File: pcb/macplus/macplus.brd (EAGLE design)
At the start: 58 x 35 mm, 9 parts, among them J1 ATX24RH

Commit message: mac plus adaptor pretty much done
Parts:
- added JP3: (no value), pinhead:1X02
- moved JP1 2.32 mm to (10.7, 25.3), turned to 270 degrees
- moved JP4 2.30 mm to (2.55, 25.4)
- moved U$2 0.55 mm to (46.6, 14.5)
- moved U$8 0.26 mm to (25.4, 14.5)
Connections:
- net GND: now also JP3.2
- net N$10: now also JP3.1
- net N$6: no longer J1.4
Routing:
- net -12V: track 83.6 -> 43.7 mm
- net N$10: track 9.00 -> 17.0 mm
- net +12V: track 71.2 -> 65.2 mm
- net +5V: track 53.1 -> 47.4 mm
- net N$6: track 44.5 -> 39.6 mm
- net N$8: track 14.6 -> 15.7 mm
- net N$7: track 9.40 -> 8.77 mm
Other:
- outline, holes or cut-outs redrawn
- board text added: "+12"
- board text added: "+5V"
- board text added: "-12"
- board text added: "BAT"
- board text added: "HS"
- board text added: "LATCH TOWARDS EDGE"
- board text added: "Macintosh 128K/512K/Plus ATX Adaptor PT0 dekuNukem Nov 2022"
- board text added: "SPK"
- board text added: "VID"
- board text added: "VS"
- board text removed: "3V3"
- board text removed: "Bob Dishwasher Cassette Rewinder"
- board text removed: "CART OK"
- board text removed: "CLK"
- board text removed: "DIO"
- board text removed: "DONE"
- board text removed: "G"
- board text removed: "Mac 128/512/Plus ATX Adaptor dekuNukem Nov 2022"
- board text removed: "NOTCH TOWARDS EDGE"
- board text removed: "POWER"
- board text removed: "RENEW"
- board text removed: "RESET"
- board text removed: "RX"
- board text removed: "SCL"
- board text removed: "SDA"
- board text removed: "TX"
- board text removed: "VCC"
- board text removed: "dekuNukem 2021"
- board text removed: "git.io/bob_rewind"

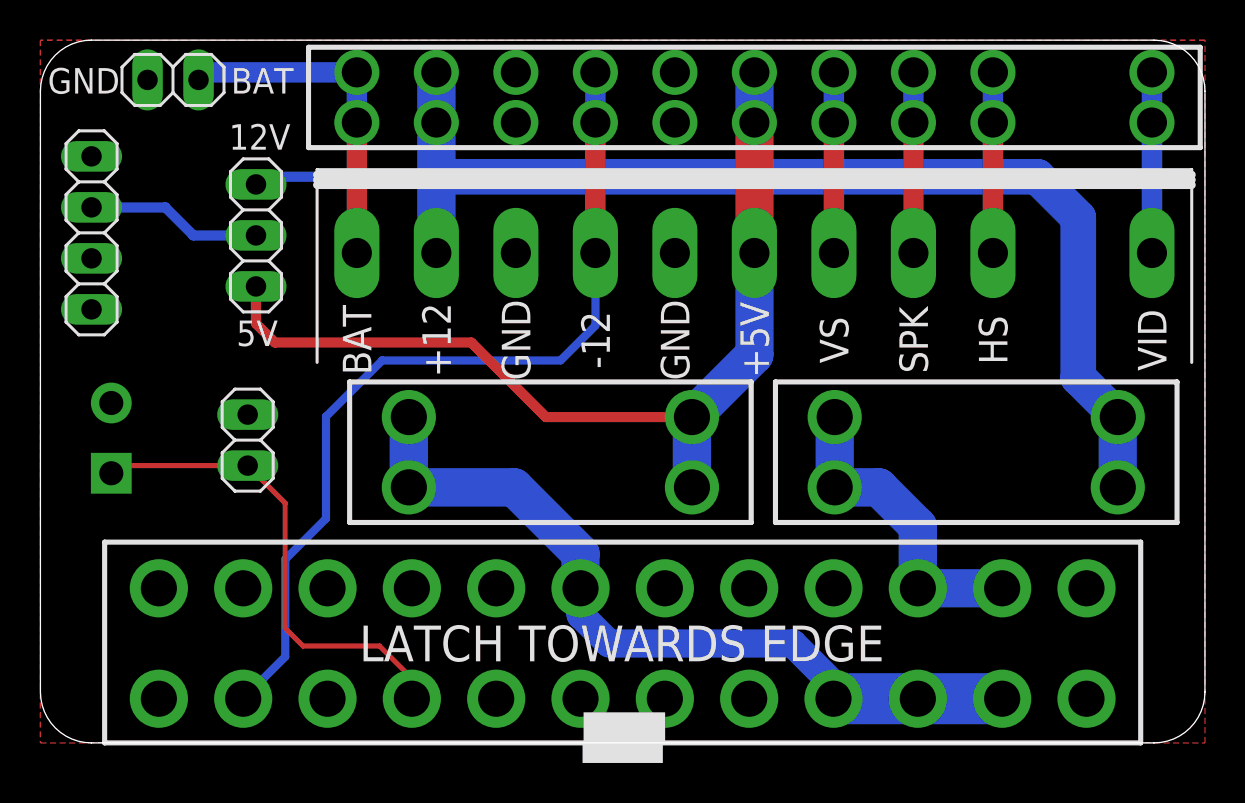
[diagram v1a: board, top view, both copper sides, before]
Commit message: updated mac plus atx adaptor
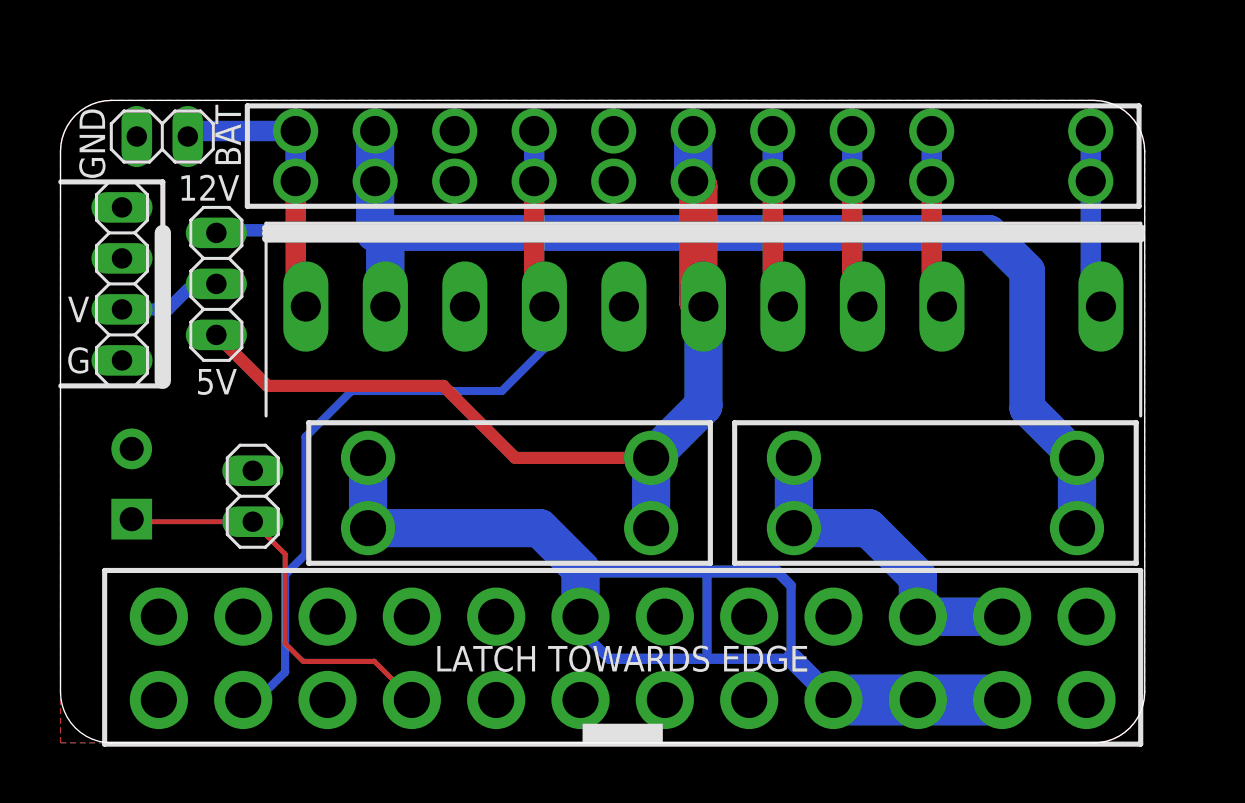
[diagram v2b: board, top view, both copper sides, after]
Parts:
- moved U$3 4.22 mm to (32.5, 29.2)
- moved U$1 3.68 mm to (33.0, 21.7)
- moved JP1 3.12 mm to (8.76, 22.9), turned to 90 degrees
- moved JP4 2.96 mm to (4.06, 22.9), turned to 270 degrees
- moved U$2 2.87 mm to (44.6, 12.4)
- moved U$8 2.87 mm to (23.4, 12.4)
- moved JP3 2.87 mm to (6.07, 30.2)
- moved JP2 2.81 mm to (10.6, 12.3)
- moved J7 2.50 mm to (4.55, 11.1)
- moved J1 0.76 mm to (29.0, 4.24)
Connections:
- net +12V: now also JP1.3; no longer JP1.1
- net +5V: now also JP1.1; no longer JP1.3
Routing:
- net N$6: track 39.6 -> 59.2 mm
- net -12V: track 43.7 -> 39.6 mm
- net N$5: track 24.2 -> 20.3 mm
- net N$7: track 8.77 -> 5.23 mm
- net N$10: track 17.0 -> 14.4 mm
- net +5V: track 47.4 -> 45.3 mm
- net N$8: track 15.7 -> 16.8 mm
- net +12V: track 65.2 -> 64.4 mm
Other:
- board size 58 x 35 mm -> 54 x 32 mm
- board text added: "+5"
- board text added: "G"
- board text added: "Macintosh 128K/512K/Plus ATX Adaptor"
- board text added: "V"
- board text added: "dekuNukem PT2 Nov22"
- board text removed: "+5V"
- board text removed: "Macintosh 128K/512K/Plus ATX Adaptor PT0 dekuNukem Nov 2022"

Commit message: updated mac SE pcb
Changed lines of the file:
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@@
 <grid distance="5" unitdist="mil" unit="mil" style="lines" multiple="1" display="no" altdistance="1" altunitdist="mil" altunit="mil"/>
 <layers>
-<layer number="1" name="Top" color="4" fill="1" visible="no" active="yes"/>
+<layer number="1" name="Top" color="4" fill="1" visible="yes" active="yes"/>
 <layer number="2" name="Route2" color="16" fill="1" visible="no" active="no"/>
 <layer number="3" name="Route3" color="17" fill="1" visible="no" active="no"/>
@@
 <layer number="14" name="Route14" color="22" fill="1" visible="no" active="no"/>
 <layer number="15" name="Route15" color="23" fill="1" visible="no" active="no"/>
-<layer number="16" name="Bottom" color="1" fill="1" visible="no" active="yes"/>
+<layer number="16" name="Bottom" color="1" fill="1" visible="yes" active="yes"/>
 <layer number="17" name="Pads" color="2" fill="1" visible="yes" active="yes"/>
 <layer number="18" name="Vias" color="2" fill="1" visible="yes" active="yes"/>
@@
 <contactref element="U$3" pad="P$12"/>
 <contactref element="U$3" pad="P$11"/>
-<wire x1="30.418" y1="10.696" x2="30.418" y2="14.196" width="1.905" layer="16"/>
-<wire x1="30.418" y1="14.196" x2="33.02" y2="16.798" width="1.905" layer="16"/>
-<wire x1="33.02" y1="16.798" x2="33.02" y2="21.733" width="1.905" layer="16"/>
-<wire x1="32.512" y1="30.476" x2="32.512" y2="27.976" width="1.905" layer="16"/>
-<wire x1="32.512" y1="27.976" x2="32.766" y2="27.722" width="1.905" layer="1"/>
-<wire x1="32.766" y1="27.722" x2="32.766" y2="21.987" width="1.905" layer="1"/>
-<wire x1="32.766" y1="21.987" x2="33.02" y2="21.733" width="1.905" layer="1"/>
+<wire x1="30.418" y1="10.696" x2="30.418" y2="14.196" width="2.54" layer="16"/>
+<wire x1="30.418" y1="14.196" x2="33.02" y2="16.798" width="2.54" layer="16"/>
+<wire x1="33.02" y1="16.798" x2="33.02" y2="21.733" width="2.54" layer="16"/>
+<wire x1="32.512" y1="30.476" x2="32.512" y2="27.976" width="1.778" layer="16"/>
+<wire x1="33.02" y1="25.436" x2="32.512" y2="25.944" width="1.905" layer="1"/>
+<wire x1="32.512" y1="27.976" x2="32.512" y2="25.944" width="2.286" layer="1"/>
+<wire x1="33.02" y1="25.436" x2="33.02" y2="21.733" width="2.286" layer="1"/>
 <wire x1="30.418" y1="14.196" x2="23.65" y2="14.196" width="0.6096" layer="1"/>
 <wire x1="23.65" y1="14.196" x2="20.066" y2="17.78" width="0.6096" layer="1"/>
@@
 <wire x1="33.1978" y1="4.191" x2="37.465" y2="4.191" width="0.508" layer="16"/>
 <wire x1="39.5" y1="2.156" x2="39.5" y2="2.138" width="1.397" layer="16"/>
-<wire x1="26.9" y1="6.288" x2="26.9" y2="8.533" width="1.905" layer="16"/>
+<wire x1="26.9" y1="6.288" x2="26.9" y2="8.533" width="2.54" layer="16"/>
 <wire x1="26.9" y1="8.533" x2="26.9" y2="8.66" width="1.905" layer="16"/>
-<wire x1="24.864" y1="10.696" x2="16.318" y2="10.696" width="1.905" layer="16"/>
-<wire x1="26.9" y1="8.66" x2="24.864" y2="10.696" width="1.905" layer="16"/>
-<wire x1="16.318" y1="10.696" x2="16.318" y2="14.196" width="1.905" layer="16"/>
+<wire x1="24.864" y1="10.696" x2="16.318" y2="10.696" width="2.54" layer="16"/>
+<wire x1="26.9" y1="8.66" x2="24.864" y2="10.696" width="2.54" layer="16"/>
+<wire x1="16.318" y1="10.696" x2="16.318" y2="14.196" width="2.54" layer="16"/>
 <wire x1="28.321" y1="4.191" x2="26.9" y2="5.612" width="0.508" layer="16"/>
 <wire x1="26.9" y1="5.612" x2="26.9" y2="6.288" width="0.508" layer="16"/>
 <wire x1="39.5" y1="2.156" x2="37.465" y2="4.191" width="1.016" layer="16"/>
 <wire x1="37.465" y1="4.191" x2="37.3888" y2="4.2672" width="0.508" layer="16"/>
-<wire x1="37.3888" y1="4.2672" x2="37.3888" y2="7.8232" width="0.4572" layer="16"/>
+<wire x1="37.3888" y1="4.2672" x2="37.3888" y2="7.8232" width="0.508" layer="16"/>
 <wire x1="37.3888" y1="7.8232" x2="36.679" y2="8.533" width="0.508" layer="16"/>
-<wire x1="36.679" y1="8.533" x2="33.1978" y2="8.533" width="0.6096" layer="16"/>
-<wire x1="33.1978" y1="8.533" x2="26.9" y2="8.533" width="0.6096" layer="16"/>
-<wire x1="33.1978" y1="8.533" x2="33.1978" y2="4.191" width="0.4572" layer="16"/>
+<wire x1="36.679" y1="8.533" x2="33.1978" y2="8.533" width="0.508" layer="16"/>
+<wire x1="33.1978" y1="8.533" x2="26.9" y2="8.533" width="0.7112" layer="16"/>
+<wire x1="33.1978" y1="8.533" x2="33.1978" y2="4.191" width="0.508" layer="16"/>
 </signal>
 <signal name="N$8">
@@
 <contactref element="JP4" pad="3"/>
 <contactref element="JP1" pad="2"/>
-<wire x1="8.763" y1="22.86" x2="7.62" y2="22.86" width="0.6096" layer="16"/>
-<wire x1="6.35" y1="21.59" x2="4.064" y2="21.59" width="0.6096" layer="16"/>
-<wire x1="7.62" y1="22.86" x2="6.35" y2="21.59" width="0.6096" layer="16"/>
+<wire x1="8.763" y1="22.86" x2="7.239" y2="22.86" width="0.6096" layer="16"/>
+<wire x1="5.969" y1="21.59" x2="4.064" y2="21.59" width="0.6096" layer="16"/>
+<wire x1="7.239" y1="22.86" x2="5.969" y2="21.59" width="0.6096" layer="16"/>
 </signal>
 </signals>

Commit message: finishing touches
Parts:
- added C2: (no value), capacitor-wima:C5B2.5
- moved J1 2.25 mm to (26.7, 4.24)
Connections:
- net +12V: now also C2.1
- net GND: now also C2.2
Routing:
- net +12V: track 64.4 -> 68.7 mm
- net N$6: track 59.2 -> 56.8 mm
- net -12V: track 39.6 -> 40.6 mm
- net N$8: track 16.8 -> 15.9 mm
- net +5V: track 45.3 -> 45.9 mm
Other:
- board text added: "+"
- board text added: "FUSE 5A MAX"

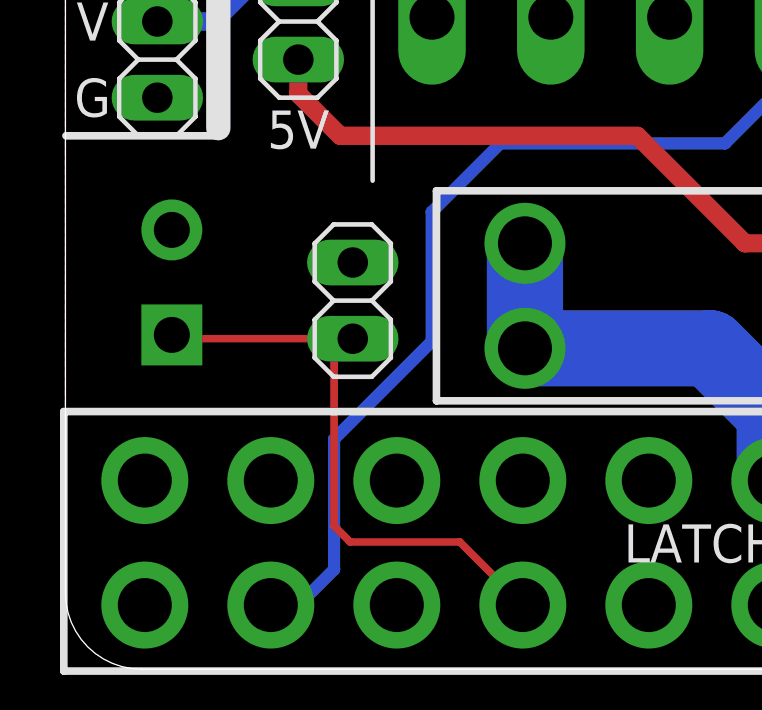
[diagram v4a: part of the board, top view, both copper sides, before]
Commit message: updated switch footprint
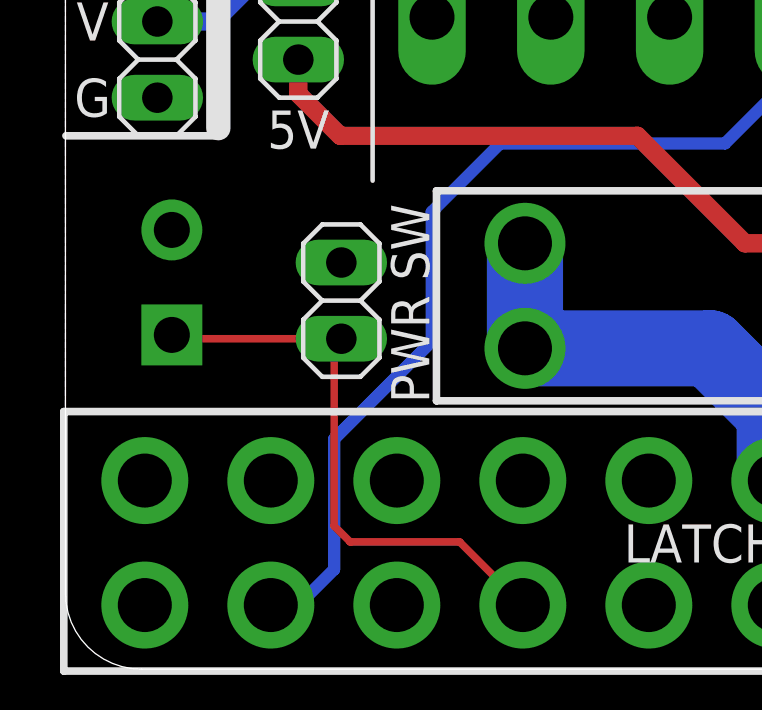
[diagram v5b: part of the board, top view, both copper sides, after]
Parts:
- moved JP2 0.38 mm to (10.2, 12.3)
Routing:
- net N$5: track 20.0 -> 19.4 mm
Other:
- board text added: "Instructions atx4vc.com"
- board text added: "PWR SW"
- board text added: "dekuNukem PD1 Nov22"
- board text removed: "Instructions: atx4vc.com"
- board text removed: "dekuNukem PT2 Nov22"
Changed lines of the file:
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@@
 <layer number="21" name="tPlace" color="7" fill="1" visible="yes" active="yes"/>
 <layer number="22" name="bPlace" color="7" fill="1" visible="yes" active="yes"/>
-<layer number="23" name="tOrigins" color="15" fill="1" visible="yes" active="yes"/>
+<layer number="23" name="tOrigins" color="15" fill="1" visible="no" active="yes"/>
 <layer number="24" name="bOrigins" color="15" fill="1" visible="yes" active="yes"/>
 <layer number="25" name="tNames" color="7" fill="1" visible="yes" active="yes"/>
@@
 <text x="30.099" y="17.526" size="1.778" layer="26" distance="35" rot="MR180" align="center">Macintosh 128K/512K/Plus ATX Adaptor</text>
 <text x="48.641" y="25.4" size="1.4224" layer="26" distance="30" rot="MR90" align="center">dekuNukem
-PT2 Nov22</text>
+PD1 Nov22</text>
 <text x="28.956" y="4.191" size="1.27" layer="25" distance="30" rot="R180" align="center">LATCH TOWARDS EDGE</text>
 <text x="9.3518" y="30.226" size="1.27" layer="25" rot="R90" align="center">BAT</text>
@@
 <wire x1="6.096" y1="27.94" x2="6.096" y2="25.654" width="0.254" layer="21"/>
 <wire x1="6.096" y1="25.4" x2="6.096" y2="18.034" width="0.8128" layer="21"/>
-<text x="44.577" y="12.446" size="1.4224" layer="26" distance="30" rot="MR180" align="center">Instructions:
+<text x="44.577" y="12.446" size="1.4224" layer="26" distance="30" rot="MR180" align="center">Instructions
 atx4vc.com</text>
 <text x="52.07" y="8.2088" size="2.1844" layer="26" rot="R180" align="center">+</text>
 <text x="23.368" y="12.446" size="1.9304" layer="26" distance="30" rot="MR0" align="center">FUSE
 5A MAX</text>
+<text x="12.4922" y="12.192" size="1.27" layer="25" rot="R270" align="center">PWR SW</text>
 </plain>
 <attributes>
@@
 <element name="U$8" library="atx_power_control" package="FUSE_HOLDER_3IN1" value="CAR_FUSE_HOLDER3IN1" x="23.368" y="12.446" smashed="yes" rot="R180"/>
 <element name="U$2" library="atx_power_control" package="FUSE_HOLDER_3IN1" value="CAR_FUSE_HOLDER3IN1" x="44.577" y="12.446" smashed="yes"/>
-<element name="JP2" library="pinhead" library_urn="urn:adsk.eagle:library:325" package="1X02" package3d_urn="urn:adsk.eagle:package:22435/2" value="" x="10.578" y="12.286" smashed="yes" rot="R90">
-<attribute name="POPULARITY" value="98" x="10.578" y="12.286" size="1.778" layer="27" rot="R90" display="off"/>
-<attribute name="VALUE" x="13.753" y="9.746" size="1.27" layer="27" rot="R90"/>
+<element name="JP2" library="pinhead" library_urn="urn:adsk.eagle:library:325" package="1X02" package3d_urn="urn:adsk.eagle:package:22435/2" value="" x="10.197" y="12.286" smashed="yes" rot="R90">
+<attribute name="POPULARITY" value="98" x="10.197" y="12.286" size="1.778" layer="27" rot="R90" display="off"/>
+<attribute name="VALUE" x="13.372" y="9.746" size="1.27" layer="27" rot="R90"/>
 </element>
 <element name="JP3" library="pinhead" library_urn="urn:adsk.eagle:library:325" package="1X02" package3d_urn="urn:adsk.eagle:package:22435/2" value="" x="6.0706" y="30.2006" smashed="yes" rot="R180">
@@
 <contactref element="JP2" pad="1"/>
 <wire x1="4.547" y1="11.143" x2="4.674" y2="11.016" width="0.254" layer="1"/>
-<wire x1="10.578" y1="11.016" x2="4.674" y2="11.016" width="0.254" layer="1"/>
-<wire x1="10.578" y1="11.016" x2="9.9568" y2="10.3948" width="0.254" layer="1"/>
-<wire x1="9.9568" y1="10.3948" x2="9.9568" y2="4.7752" width="0.254" layer="1"/>
+<wire x1="10.197" y1="11.016" x2="4.674" y2="11.016" width="0.254" layer="1"/>
+<wire x1="10.197" y1="11.016" x2="9.9568" y2="10.7758" width="0.254" layer="1"/>
+<wire x1="9.9568" y1="10.7758" x2="9.9568" y2="4.7752" width="0.254" layer="1"/>
 <wire x1="9.9568" y1="4.7752" x2="10.4902" y2="4.2418" width="0.254" layer="1"/>
 <wire x1="14.1422" y1="4.2418" x2="16.246" y2="2.138" width="0.254" layer="1"/>
